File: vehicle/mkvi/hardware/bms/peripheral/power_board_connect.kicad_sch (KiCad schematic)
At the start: 1 part, among them J3 Automotive_M.2_Edge_Connector

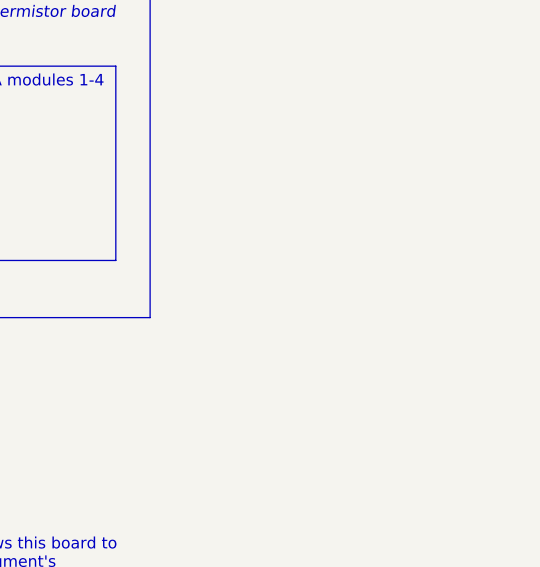
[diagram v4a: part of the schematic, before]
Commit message: Begin layout and related minor edits to schematics
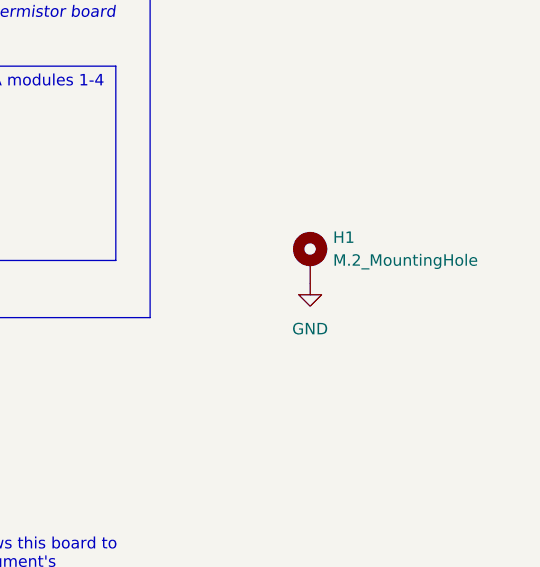
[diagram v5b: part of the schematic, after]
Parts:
- added H1: M.2_MountingHole, OEM:M.2_Mount, symbol formula:M.2_MountingHole
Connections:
- net GND: now also H1.1
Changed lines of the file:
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@@
     (effects (font (size 1.27 1.27)) (justify right))
+  )
+  (symbol (lib_id "formula:M.2_MountingHole") (at 233.68 82.55 0) (unit 1)
+    (in_bom yes) (on_board yes) (fields_autoplaced)
+    (property "Reference" "H1" (id 0) (at 236.22 80.0099 0)
+      (effects (font (size 1.27 1.27)) (justify left))
+    )
+    (property "Value" "M.2_MountingHole" (id 1) (at 236.22 82.5499 0)
+      (effects (font (size 1.27 1.27)) (justify left))
+    )
+    (property "Footprint" "OEM:M.2_Mount" (id 2) (at 233.68 82.55 0)
+      (effects (font (size 1.27 1.27)) hide)
+    )
+    (property "Datasheet" "~" (id 3) (at 233.68 82.55 0)
+      (effects (font (size 1.27 1.27)) hide)
+    )
+    (pin "1")
   )
   (symbol (lib_id "formula:Automotive_M.2_Edge_Connector") (at 157.48 78.74 0) (unit 1)
@@
       (effects (font (size 1.27 1.27)) hide)
     )
+    (pin "1")
+  )
+  (symbol (lib_id "power:GND") (at 233.68 85.09 0) (unit 1)
+    (in_bom yes) (on_board yes) (fields_autoplaced)
+    (property "Reference" "#PWR?" (id 0) (at 233.68 91.44 0)
+      (effects (font (size 1.27 1.27)) hide)
+    )
+    (property "Value" "GND" (id 1) (at 233.68 90.17 0))
+    (property "Footprint" "" (id 2) (at 233.68 85.09 0)
+      (effects (font (size 1.27 1.27)) hide)
+    )
+    (property "Datasheet" "" (id 3) (at 233.68 85.09 0)
+      (effects (font (size 1.27 1.27)) hide)
+    )

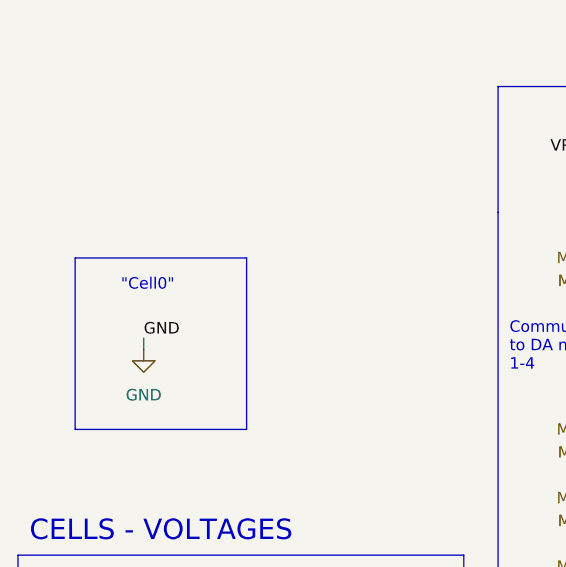
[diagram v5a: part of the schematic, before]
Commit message: Add notes to schematic
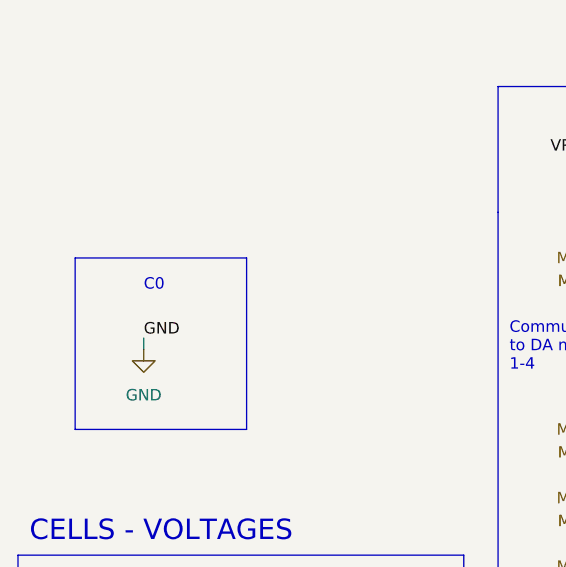
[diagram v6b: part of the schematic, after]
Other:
- note added: "C0"
- note removed: ""Cell0""
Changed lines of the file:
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@@
     (stroke (width 0) (type default) (color 0 0 0 0))
   )
-  (text "\"Cell0\"" (at 80.01 53.34 0)
+  (text "C0" (at 82.55 53.34 0)
     (effects (font (size 1.27 1.27)) (justify left bottom))
   )

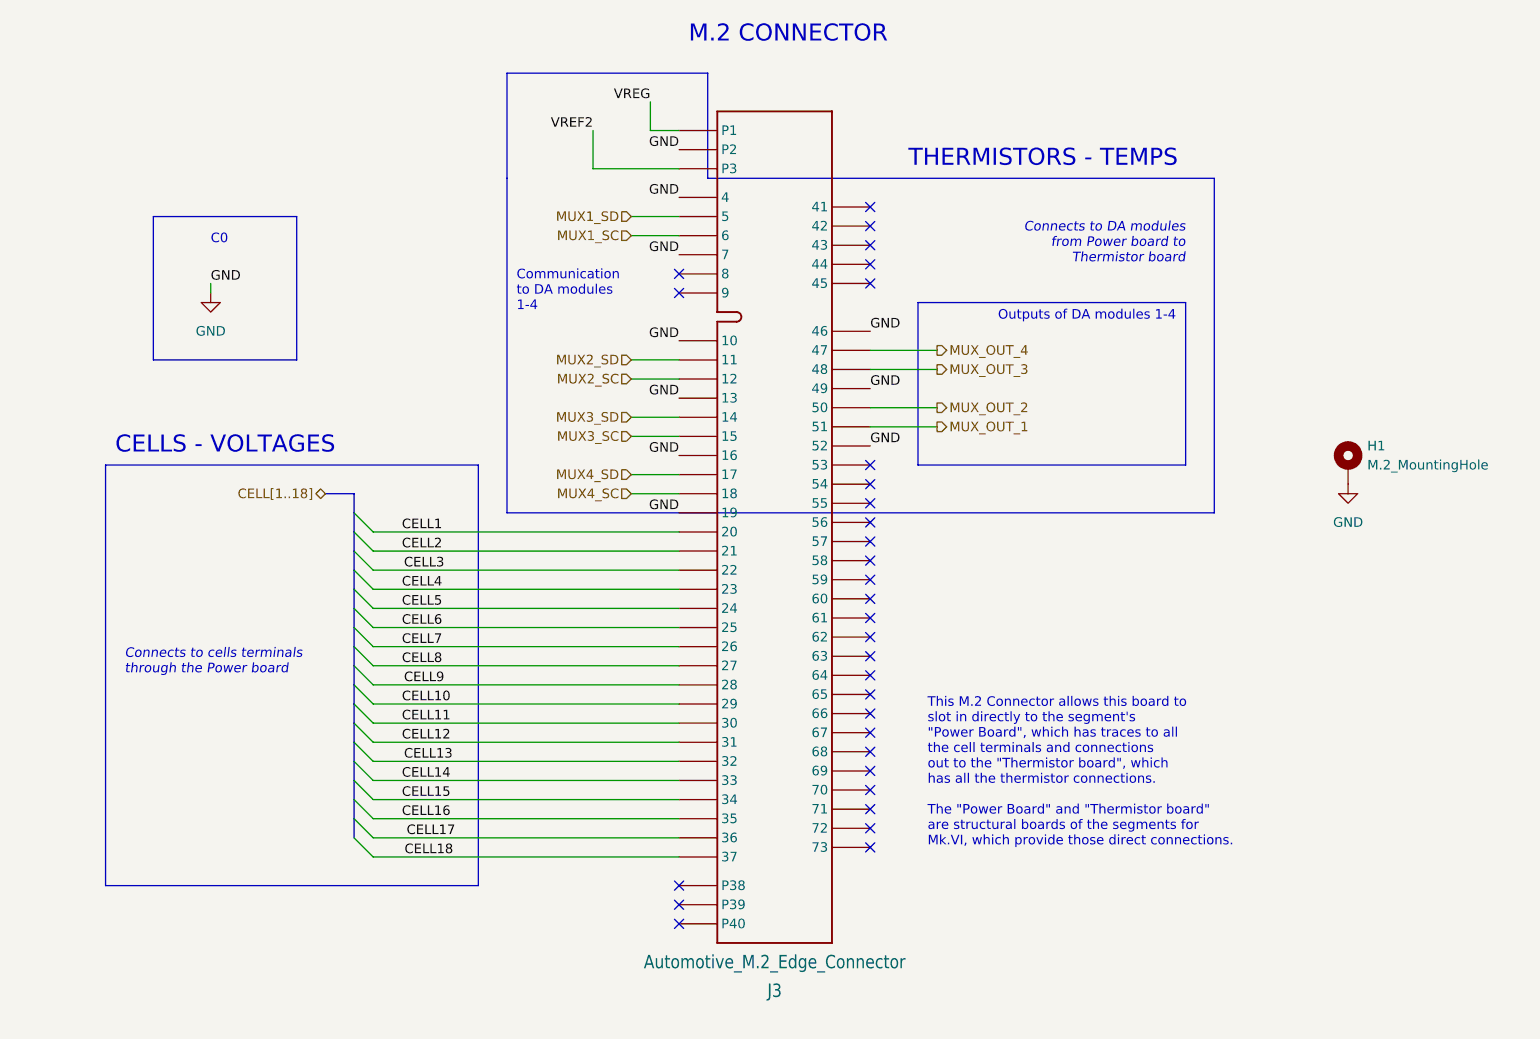
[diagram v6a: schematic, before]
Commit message: Add I2C pull-up resistors to schem and work on layout
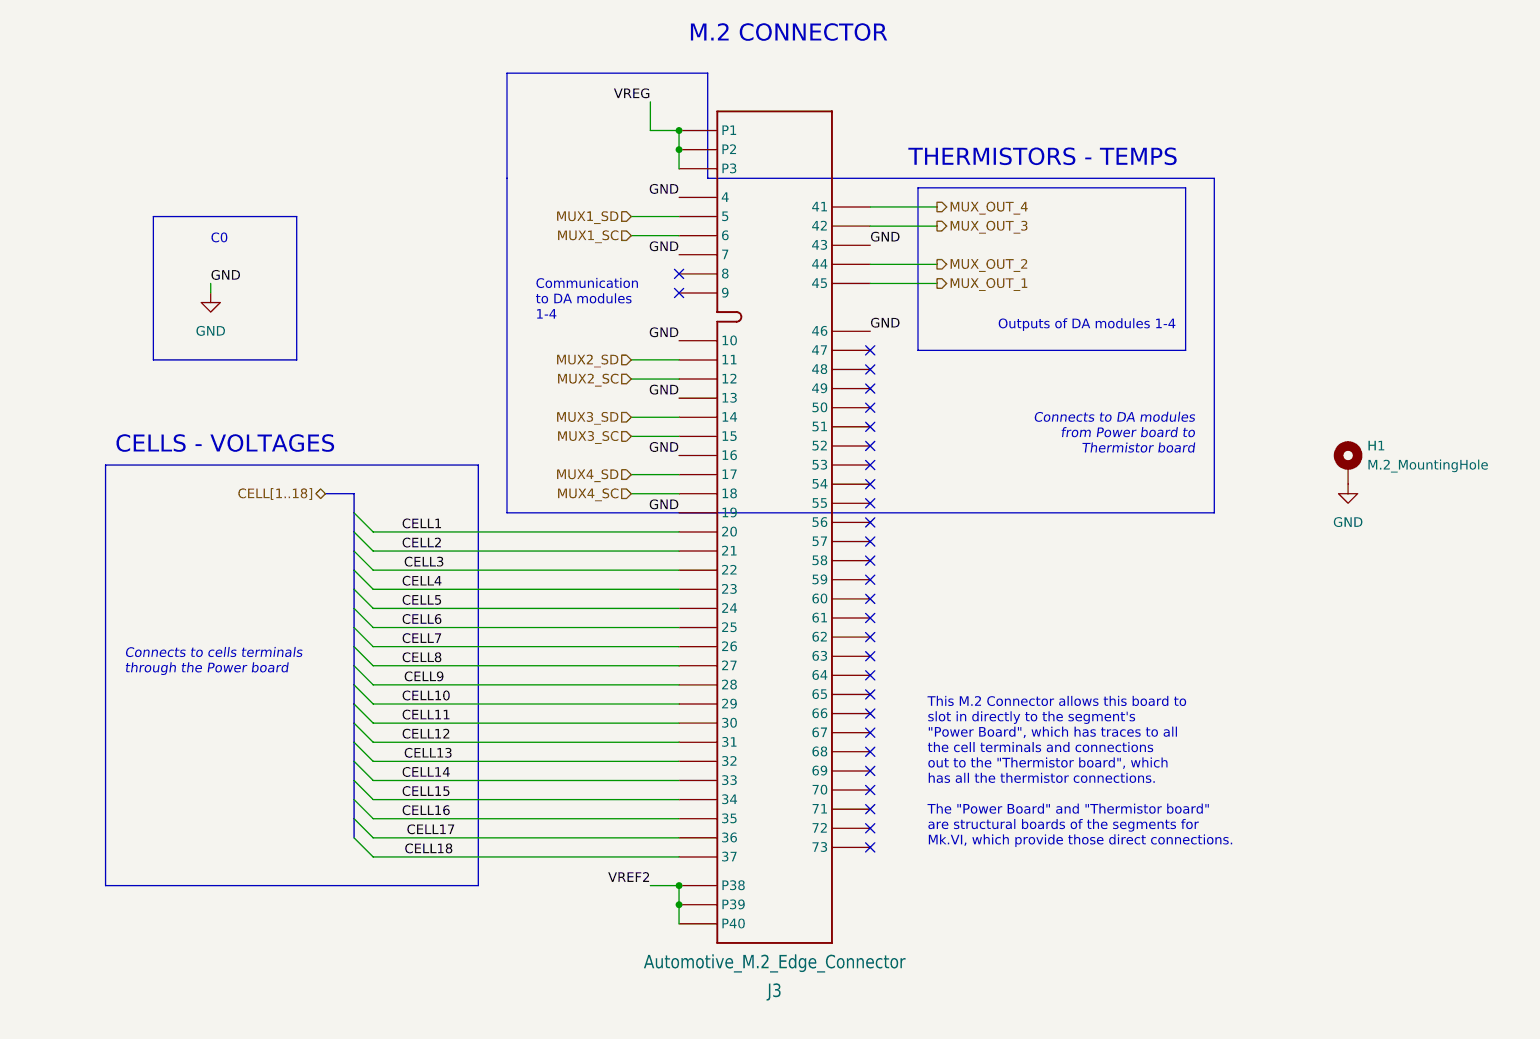
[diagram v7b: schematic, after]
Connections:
- net GND: now also J3.43; no longer J3.49, J3.52, J3.P2
- net MUX_OUT_1: now also J3.45; no longer J3.51
- net MUX_OUT_2: now also J3.44; no longer J3.50
- net MUX_OUT_3: now also J3.42; no longer J3.48
- net MUX_OUT_4: now also J3.41; no longer J3.47
- net VREF2: now also J3.P38, J3.P39, J3.P40; no longer J3.P3
- net VREG: now also J3.P2, J3.P3
- no-connect marks 31 -> 29

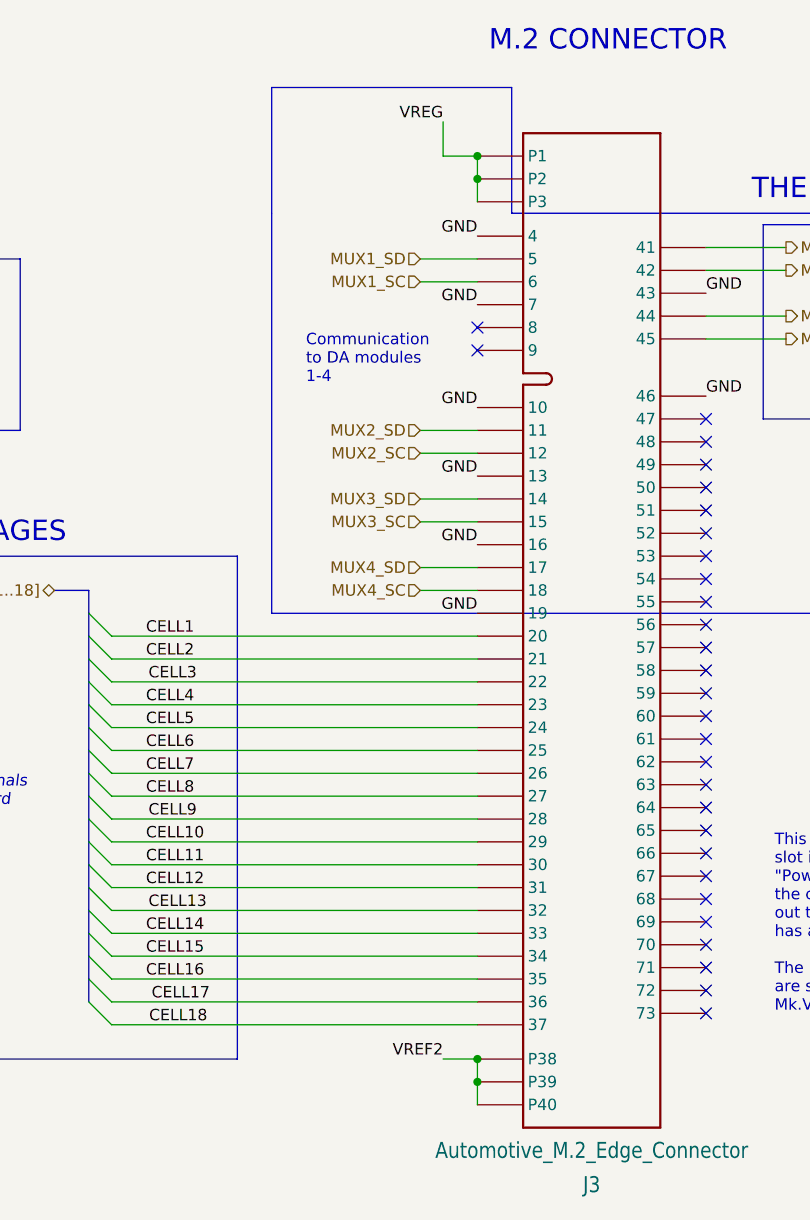
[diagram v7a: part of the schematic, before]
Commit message: Reorganize balance circuits for space, fix power label connections
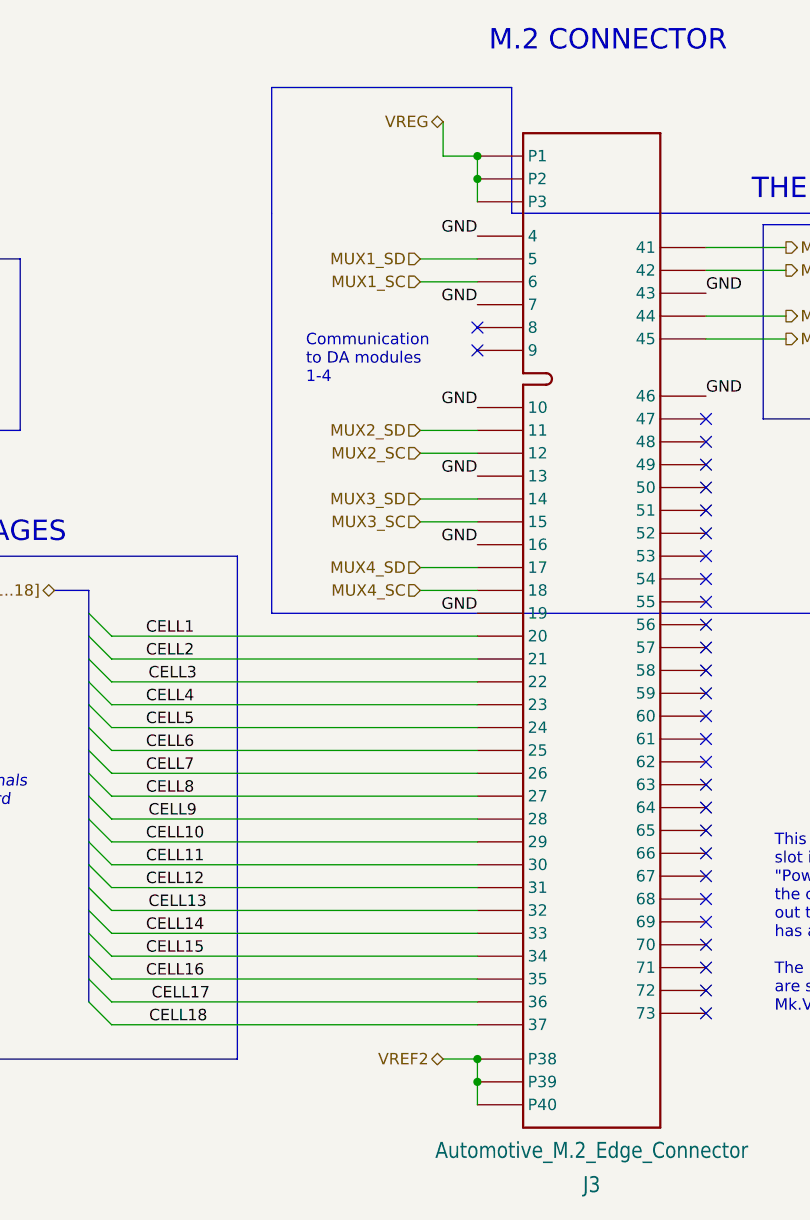
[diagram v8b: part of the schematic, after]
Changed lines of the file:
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@@
     (effects (font (size 1.27 1.27)) (justify left bottom))
-  )
-  (label "VREG" (at 140.97 34.29 180)
-    (effects (font (size 1.27 1.27)) (justify right bottom))
   )
   (label "CELL4" (at 107.95 99.06 0)
@@
   (label "CELL10" (at 107.95 114.3 0)
     (effects (font (size 1.27 1.27)) (justify left bottom))
-  )
-  (label "VREF2" (at 140.97 138.43 180)
-    (effects (font (size 1.27 1.27)) (justify right bottom))
   )
   (label "CELL6" (at 107.95 104.14 0)
@@
     (effects (font (size 1.27 1.27)) (justify right))
   )
+  (hierarchical_label "VREF2" (shape bidirectional) (at 140.97 138.43 180)
+    (effects (font (size 1.27 1.27)) (justify right))
+  )
   (hierarchical_label "MUX4_SC" (shape input) (at 138.43 86.36 180)
     (effects (font (size 1.27 1.27)) (justify right))
@@
     (effects (font (size 1.27 1.27)) (justify right))
   )
+  (hierarchical_label "VREG" (shape bidirectional) (at 140.97 34.29 180)
+    (effects (font (size 1.27 1.27)) (justify right))
+  )
